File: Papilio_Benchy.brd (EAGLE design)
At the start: 101.6 x 90.2 mm, 134 parts, among them IC1 FT2232H, IC2 93C46, J1 USB MICRO, J4 HDMI-TYPE-A-RECEPTICALFCI1002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, SW1 SWITCH-2CH-6P-3010010P1, SW2 EVQQ2, T1 MOSFET-NCHANNELSMD, U1 ATMEGA32U4-XUMU, U11 PCA9306, U2 LTC3419EMS, U5 ARDUINO_MEGA_SHIELD, X2 12MHz, Y1 16MHz KX-7

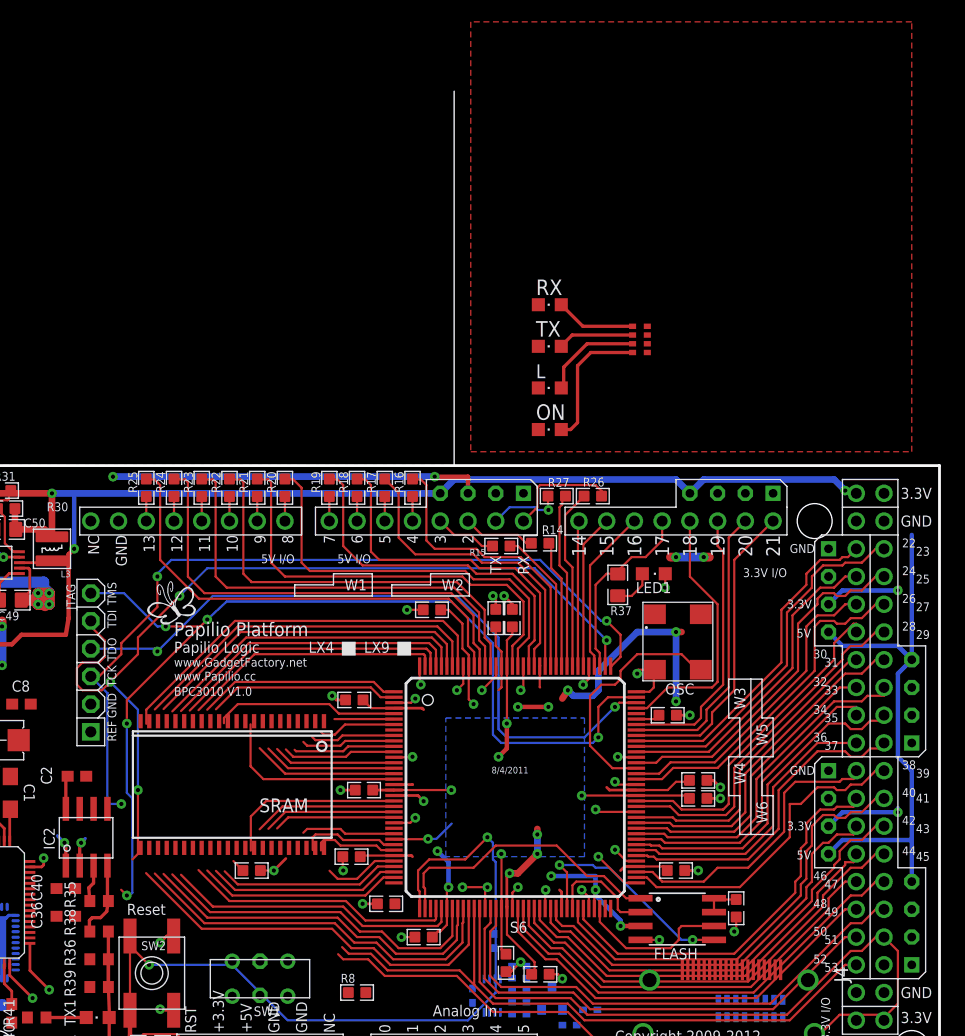
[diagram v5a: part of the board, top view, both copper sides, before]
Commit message: Schematic Cleanup - Ready for routing...
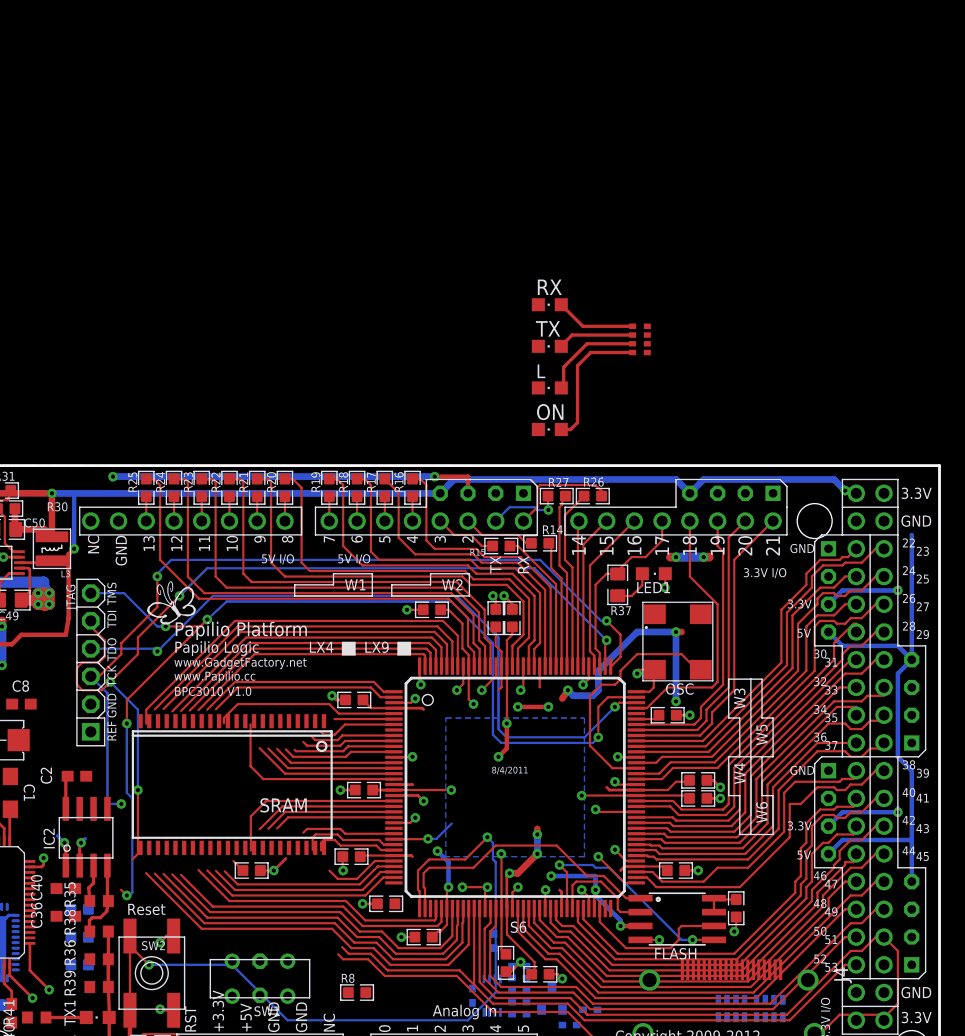
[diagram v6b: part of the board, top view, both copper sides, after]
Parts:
- added R47, R48, R49: 390, GadgetFactory:0603
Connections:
- net FPGA_RXD renamed MEGA_D1
- net FPGA_TXD renamed MEGA_D0
- removed net AD4: IC1.21
- removed net BD4: IC1.43
- removed net FPGA_SCL: R12.2, U11.3
- removed net FPGA_SDA: R13.2, U11.4
- removed net NC1: S6.22
- removed net NC2: S6.8
- new net AD4-DTR: IC1.21, S6.22
- new net BD4-DTR: IC1.43, S6.8
- new net N$10: R49.2, U1.9
- new net N$11: R48.2, U1.10
- new net N$12: R47.2, U1.11
- net 3V3: now also SRAM.11, SRAM.33, U5.3V3@1, U5.3V3@2, U5.3V3@3, U5.3V3@4
- net GND: now also U5.GND@5, U5.GND@6
- net MEGA_D40: now also R47.1
- net MEGA_D41: now also R48.1
- net MEGA_D42: now also R49.1
- net MEGA_D43: now also R13.2, U11.4
- net MEGA_D44: now also R12.2, U11.3
- net MEGA_D51: no longer U1.9
- net MEGA_D52: no longer U1.10
- net MEGA_D53: no longer U1.11
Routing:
- net NC1: track 13.2 -> 0.00 mm
- net AD4-DTR: track 0.00 -> 13.2 mm
- removed copper zone on layer 1, net GND
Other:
- board size 101.6 x 90.2 mm -> 101.6 x 55.9 mm

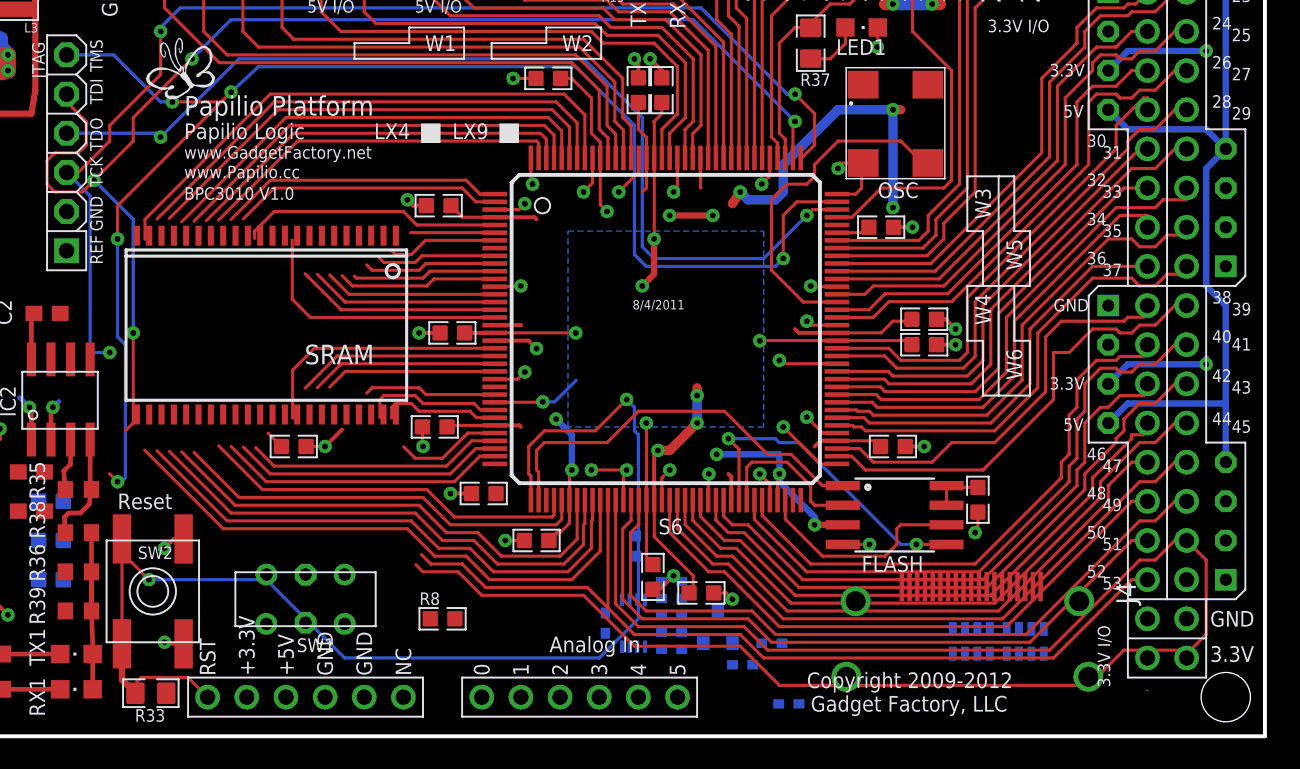
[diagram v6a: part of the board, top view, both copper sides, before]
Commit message: Sram initiallly routed.
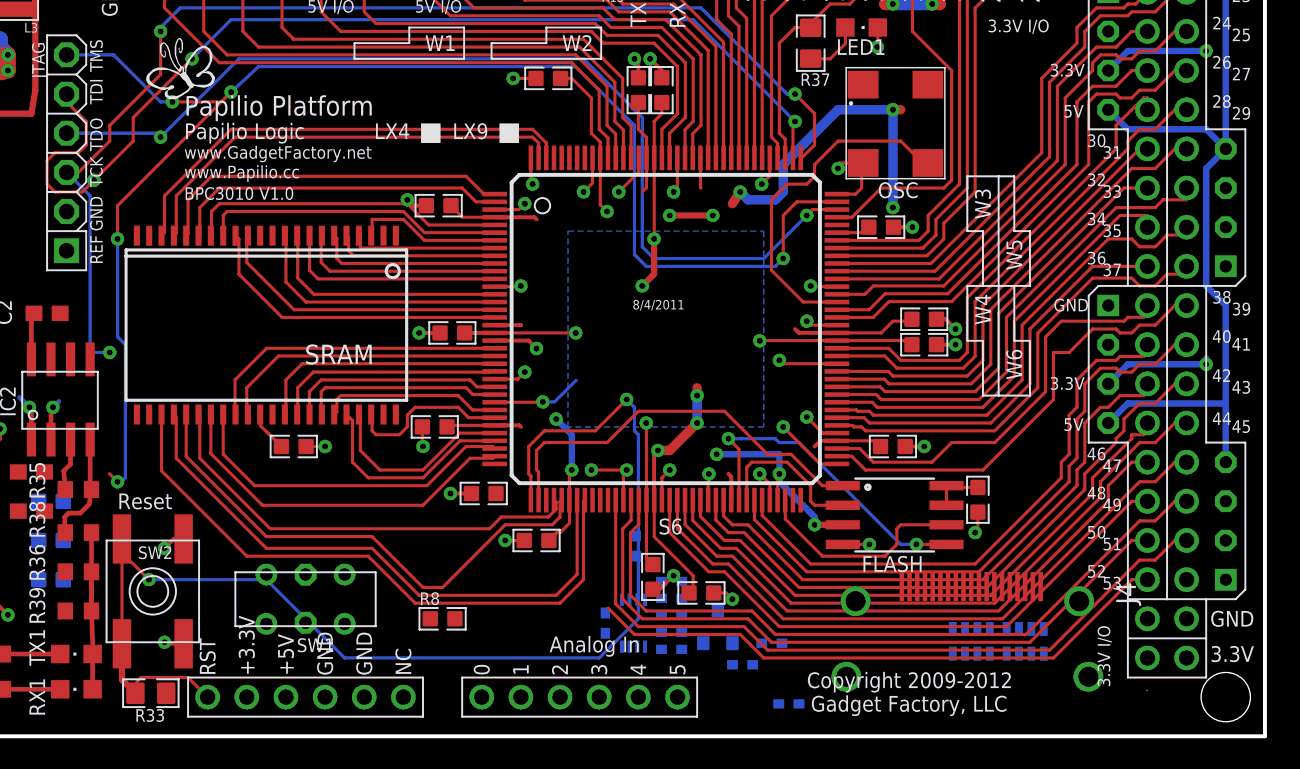
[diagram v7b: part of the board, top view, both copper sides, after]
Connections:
- removed net ARDUINO_RESET: D2.A, R7.1, S6.34, U1.13
- new net ARD_RESET: D2.A, R7.1, S6.139, U1.13
- net A0: now also S6.7; no longer S6.6
- net A1: now also S6.8; no longer S6.7
- net A10: now also S6.43; no longer S6.46
- net A11: now also S6.41; no longer S6.45
- net A12: now also S6.40; no longer S6.44
- net A13: now also S6.35; no longer S6.43
- net A14: now also S6.34; no longer S6.41
- net A15: now also S6.27; no longer S6.29
- net A16: now also S6.29; no longer S6.30
- net A17: now also S6.33; no longer S6.32
- net A18: now also S6.32; no longer S6.40
- net A19: now also S6.44; no longer S6.35
- net A20: now also S6.30; no longer S6.33
- net A5: now also S6.5; no longer S6.141
- net A6: now also S6.2; no longer S6.140
- net A7: now also S6.1; no longer S6.139
- net A8: now also S6.143; no longer S6.138
- net A9: now also S6.142; no longer S6.137
- net AD4-DTR: now also S6.45; no longer S6.22
- net BD0_MPSSE_TCK: now also S6.46; no longer S6.21
- net BD1_MPSSE_TDI: now also S6.140; no longer S6.24
- net BD2_MPSSE_TDO: now also S6.141; no longer S6.23
- net BD3_MPSSE_TMS: now also S6.138; no longer S6.26
- net BD4-DTR: now also S6.137; no longer S6.8
- net D4: now also S6.21; no longer S6.5
- net D5: now also S6.22; no longer S6.2
- net D6: now also S6.23; no longer S6.1
- net D7: now also S6.24; no longer S6.143
- net OE: now also S6.26; no longer S6.27
- net WE: now also S6.6; no longer S6.142
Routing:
- net MEGA_D51: track 110.5 -> 48.0 mm
- net ARDUINO_RESET: track 27.3 -> 0.00 mm
- net A19: track 18.7 -> 40.4 mm
- net MEGA_D52: track 59.0 -> 38.4 mm
- net AD1-JTAG_TDI: track 85.5 -> 68.0 mm, vias 4 -> 3
- net BD0_MPSSE_TCK: track 16.8 -> 0.00 mm
- net AD4-DTR: track 13.2 -> 0.00 mm
- net BD2_MPSSE_TDO: track 12.1 -> 0.00 mm
- net A18: track 24.7 -> 12.6 mm
- net BD1_MPSSE_TDI: track 11.1 -> 0.00 mm
- net ARD_RESET: track 0.00 -> 9.56 mm
- net D7: track 23.9 -> 15.0 mm
- net A7: track 31.3 -> 23.4 mm
- net A13: track 31.4 -> 23.6 mm
- net A6: track 29.6 -> 21.9 mm
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
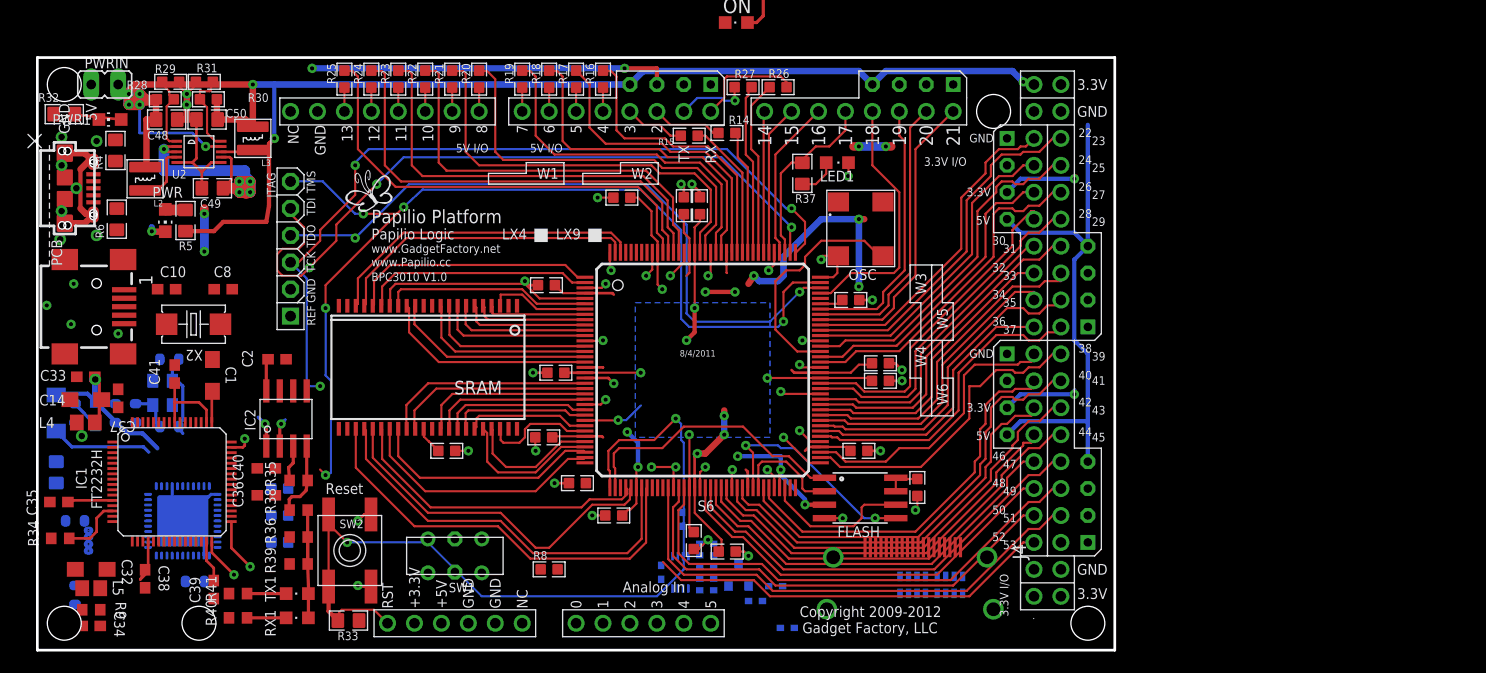
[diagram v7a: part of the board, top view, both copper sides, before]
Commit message: 4 layers and all power planes fixed
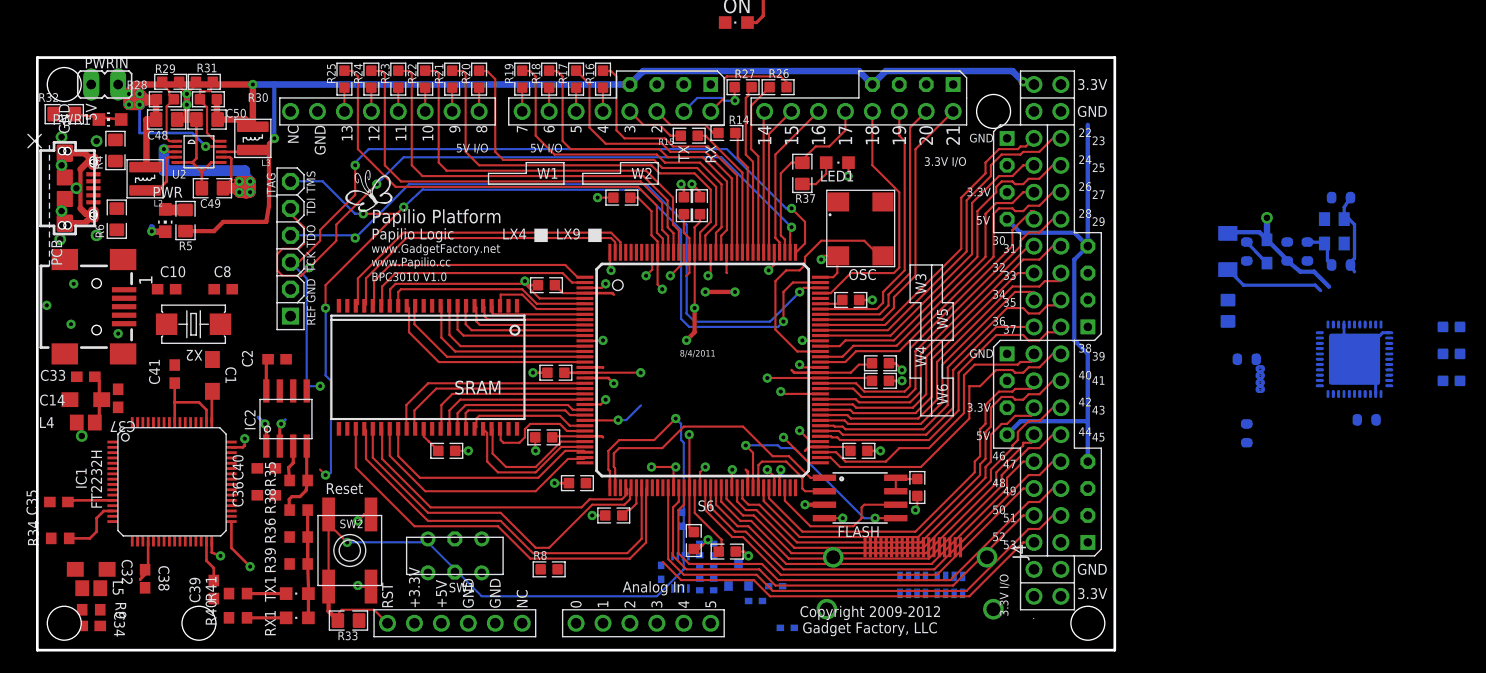
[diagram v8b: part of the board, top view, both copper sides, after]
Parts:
- moved C11 111.5 mm to (122.9, 42.7)
- moved C4 111.5 mm to (125.3, 21.7)
- moved C5 111.5 mm to (114.0, 37.6)
- moved C6 111.5 mm to (114.0, 20.4)
- moved C7 111.5 mm to (114.0, 27.4)
- moved R1 111.5 mm to (122.9, 36.3)
- moved R2 111.5 mm to (115.3, 25.2)
- moved R3 111.5 mm to (115.3, 25.9)
- moved U1 111.5 mm to (124.2, 27.4)
- moved Y1 111.5 mm to (122.3, 39.5)
- moved C3 111.5 mm to (117.9, 37.6)
- moved C9 111.5 mm to (119.8, 37.6)
- moved D2 111.5 mm to (112.3, 37.6)
- moved L6 111.5 mm to (116.0, 37.6)
- moved R47 111.5 mm to (133.3, 30.5)
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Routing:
- net 3V3: track 206.2 -> 104.6 mm, vias 28 -> 11
- net AC5: track 4.28 -> 2.20 mm
- added copper zone on layer 3, net 1V2
- added copper zone on layer 3, net 3V3
- added copper zone on layer 2, net GND
- removed copper zone on layer 16, net 1V2
